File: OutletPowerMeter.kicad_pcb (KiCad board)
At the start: 2 copper layers, 170.2 x 66.2 mm, 98 parts, among them J1 TB002-500-03BE, J2 TB002V-500-03BE, J3 OLED, J4 Programmer, J5 TB002V-500-02BE, SW1 KSC441GDCT70SHLFS, T1 115V / 9V, U1 ESP32-DEVKITC-32D, U10 ADG3304BRUZ-REEL7, U11 VX7803-500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

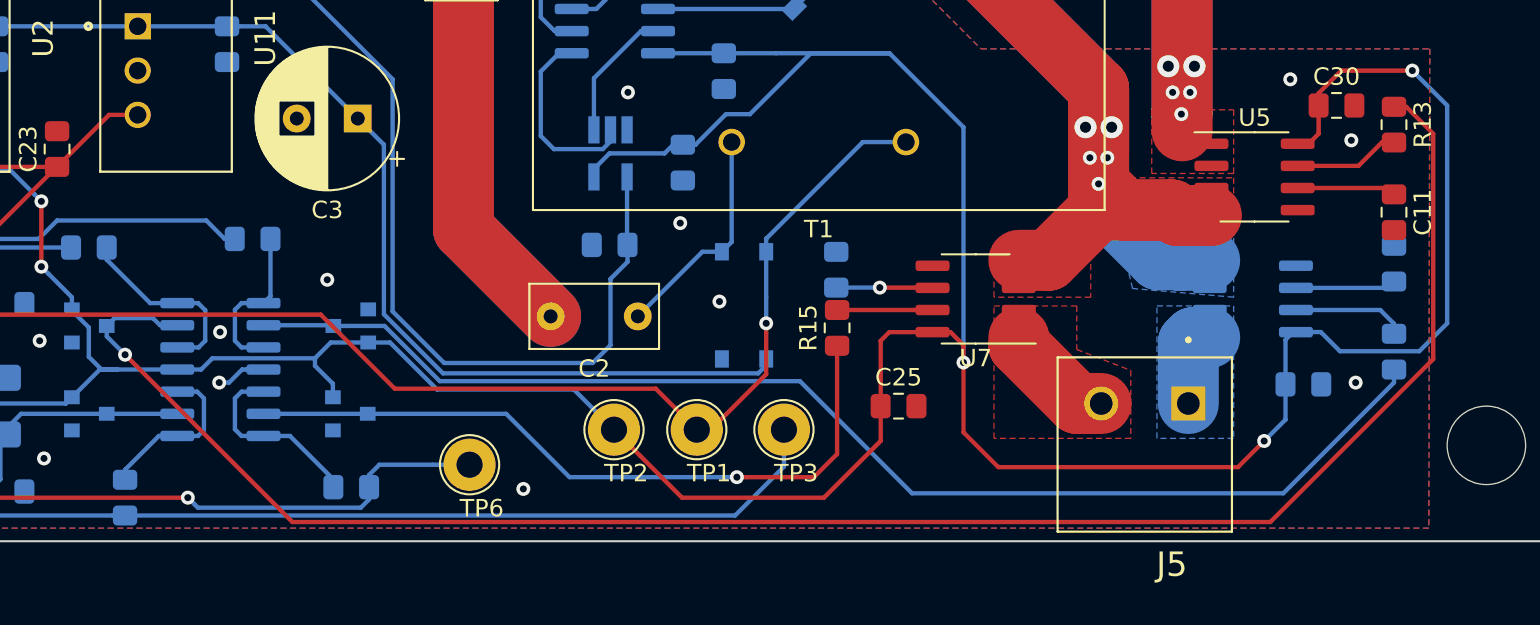
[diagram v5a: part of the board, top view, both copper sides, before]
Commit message: Updated schematic to make it more 'linear' and added the 27k resistors for power factor circuitry
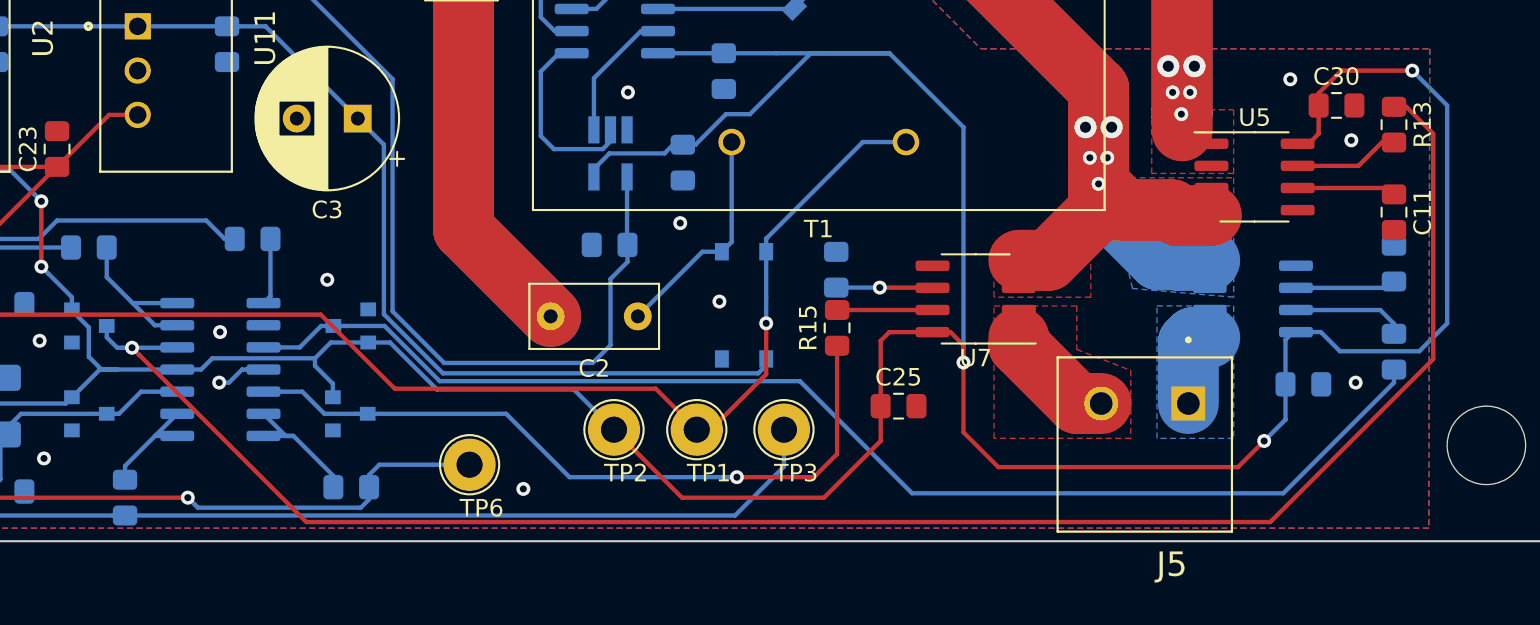
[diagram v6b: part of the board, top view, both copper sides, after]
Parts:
- turned D1 to 90 degrees
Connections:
- D1 pad 1: Net-(C2-Pad1) -> Net-(C22-Pad1)
- D1 pad 2: 9V -> GND
- D1 pad 3: Net-(C22-Pad1) -> 9V
- D1 pad 4: GND -> Net-(C2-Pad1)
- U3 pad 10: Net-(R17-Pad2) -> Net-(D4-Pad3)
- U3 pad 12: Net-(R18-Pad2) -> Net-(D5-Pad3)
- U3 pad 13: Net-(D5-Pad3) -> Net-(R18-Pad2)
- U3 pad 2: Net-(C6-Pad2) -> Net-(R12-Pad2)
- U3 pad 3: Net-(R12-Pad2) -> Net-(C6-Pad2)
- U3 pad 5: Net-(R16-Pad2) -> Net-(D3-Pad3)
- U3 pad 6: Net-(D3-Pad3) -> Net-(R16-Pad2)
- U3 pad 9: Net-(D4-Pad3) -> Net-(R17-Pad2)
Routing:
- net Net-(R17-Pad2): track 9.19 -> 3.85 mm
- net Net-(R12-Pad2): track 9.55 -> 6.29 mm
- net Net-(R18-Pad2): track 10.8 -> 7.85 mm
- net Net-(D3-Pad3): track 105.2 -> 103.4 mm
- net Net-(R16-Pad2): track 11.1 -> 9.44 mm
- net Net-(D5-Pad3): track 41.2 -> 41.7 mm
- net Net-(C6-Pad2): track 17.9 -> 18.4 mm
